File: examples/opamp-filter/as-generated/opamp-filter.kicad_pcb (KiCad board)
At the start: 2 copper layers, 58 x 42 mm, 22 parts, among them J1 IN, J2 5V, J3 OUT, U1 MCP6001R, U2 MCP6001R

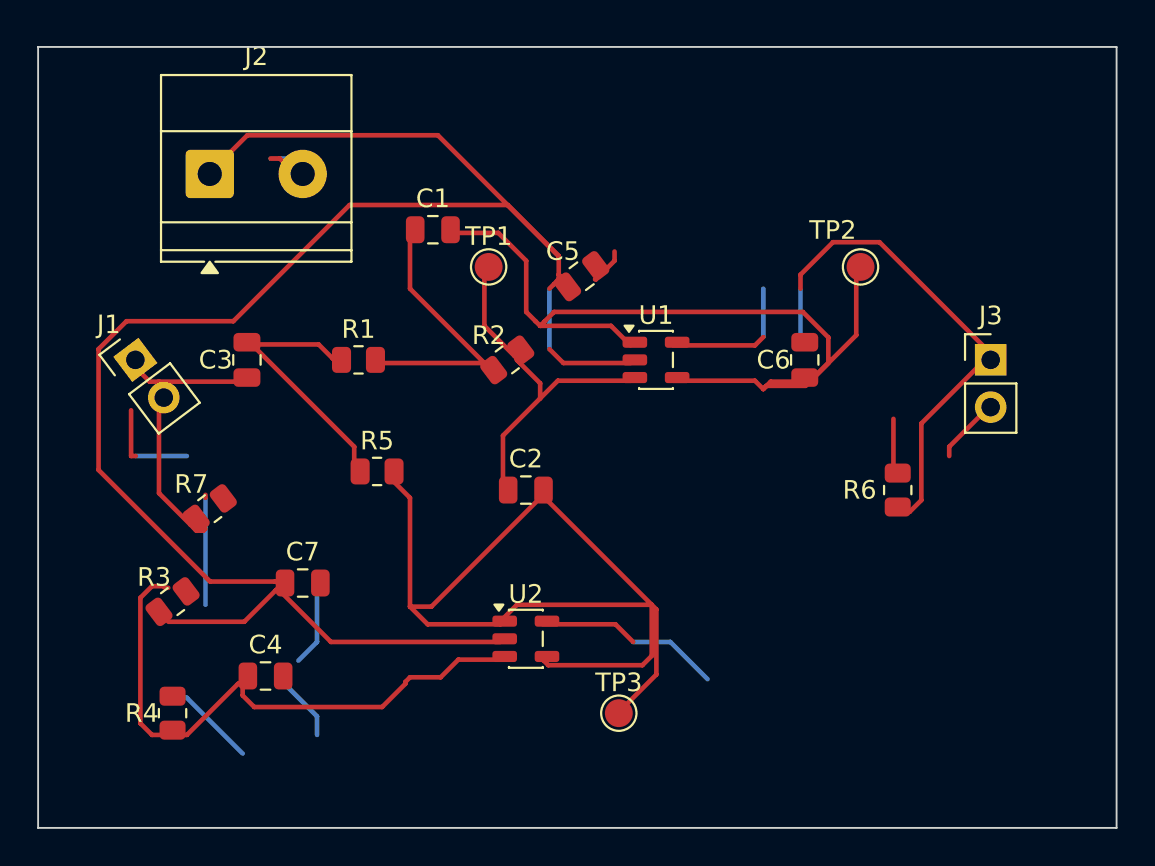
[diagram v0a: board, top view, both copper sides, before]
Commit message: Let a link finish on its own net's copper instead of the pad it names
Every junction on these boards sat on a pad, because a pad was the only
place the router was allowed to stop: a net with three branches funnelled
all three into one 0402, and the reviewer circled the result - converging
diagonals meeting on C15. People do not draw that; they tap the trunk at
the nearest point.

So the search may now end on any cell whose centre lies exactly on the
net's own copper (a tee), with two guards that took one broken board each
to learn: only copper already joined to the link's endpoint counts, or the
named pad is left unconnected; and only a pad-named endpoint may be teed
away from, because a link aimed at a bare coordinate is aimed at the
stated end of a trunk someone drew, and stopping short strands the
trunk's tail. A landing mid-segment is inserted into the trunk's points as
a stated corner, so the reshaping passes pin the join like any other.

The op-amp board shows the effect: 12% less copper, fewer corners, longer
strokes, same connectivity - DRC clean, gates clean, zero crossings on all
four regenerated boards.

Co-Authored-By: Claude Fable 5 <noreply@anthropic.com>
Claude-Session: https://claude.ai/code/session_01DUj7Ltu92tWg159mCSacwY
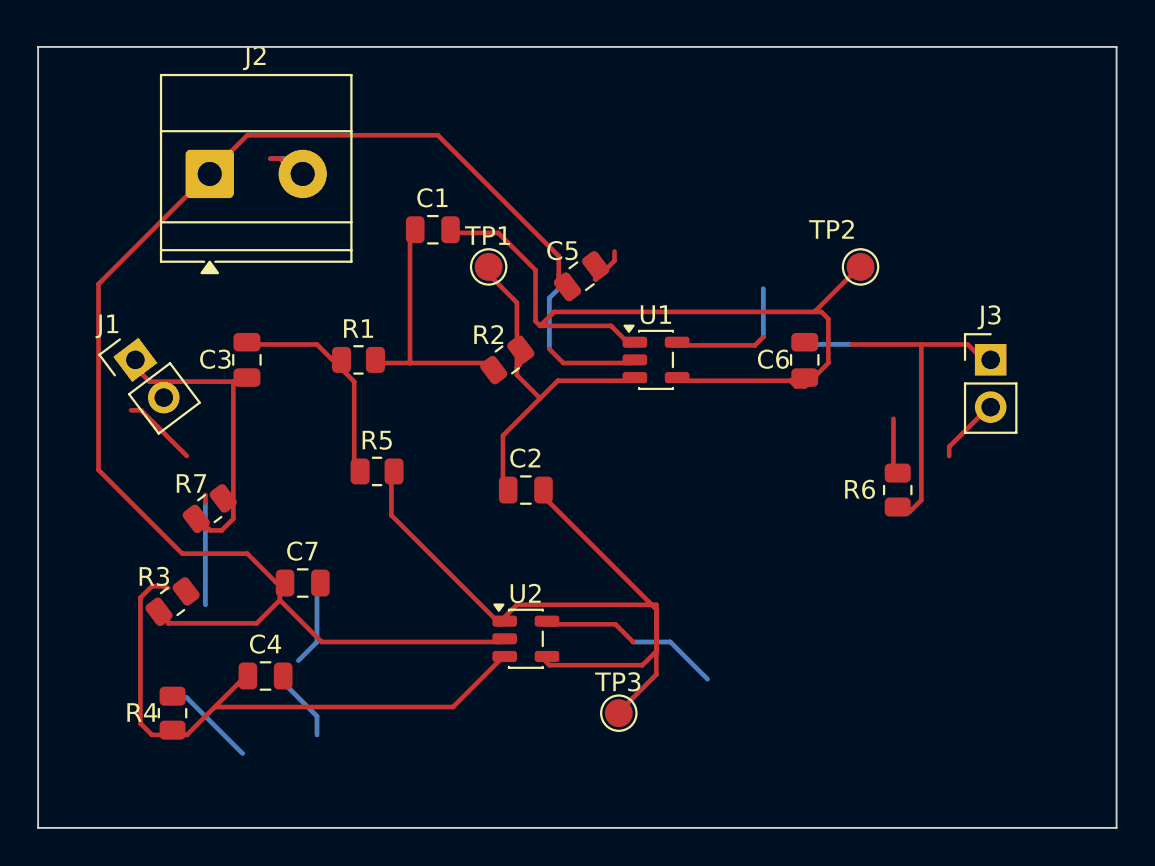
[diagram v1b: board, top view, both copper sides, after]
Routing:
- net +5V: track 100.9 -> 83.2 mm
- net /VREF: track 55.6 -> 44.1 mm
- net /OUT_AC: track 28.4 -> 20.6 mm
- net /OUT: track 50.7 -> 44.6 mm
- net /IN_DC: track 15.1 -> 12.4 mm
- net /X: track 14.9 -> 13.2 mm
- net GND: track 54.5 -> 53.0 mm

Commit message: Treat the ground plane as part of the drawing
Six reviewer circles, five of them the plane seen from different corners.
The pour now stops 1.2 mm inside the outline so an edge-hugging trace
keeps shell copper outside it; dead-end tongues narrower than 0.9 mm
retract instead of tapering to an acid-trap point in a bent corner; every
piece of the front pour over 8 mm2 holds a stitching via of its own,
placed before the orphan drop so a fenced-off strip gets a via instead of
staying a blank; and zone clearance comes down from 0.4 to 0.25, which is
what lets the plane flow between a 2.54 mm header's pins instead of
slotting the board top to bottom.

The round-twelve tee learns one manner: within two millimetres of the
goal it stands aside, so a rail flows through a bypass capacitor's pad
instead of feeding it by a stub - the carrier's bulk capacitor also moves
onto the VSYS run it was a millimetre south of. And
readability.margin_intrusion now measures symbol fields, power symbols
included: zero findings across KiCad's 18 demo sheets, one real catch on
our own motor sheet, whose power connector - like the FPGA board's -
moves in from the sheet edge so its printed name clears the frame.

Co-Authored-By: Claude Fable 5 <noreply@anthropic.com>
Claude-Session: https://claude.ai/code/session_01DUj7Ltu92tWg159mCSacwY
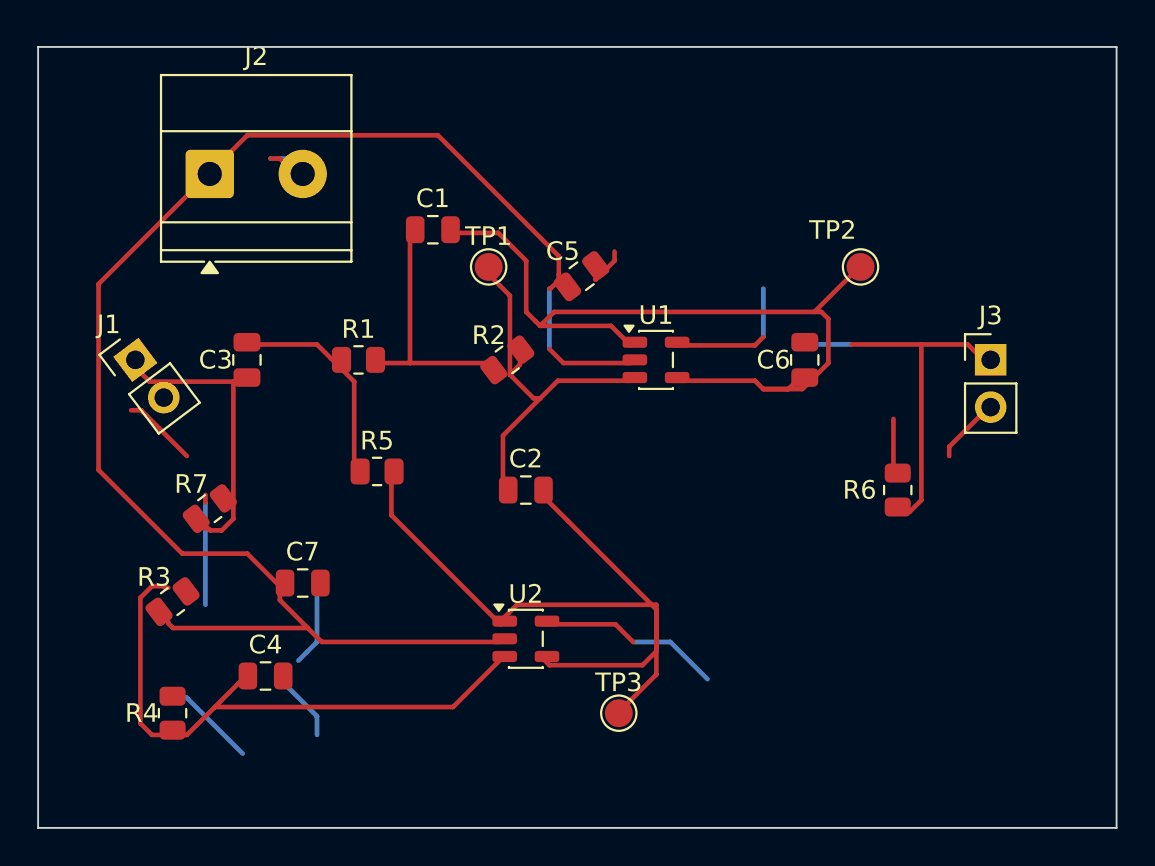
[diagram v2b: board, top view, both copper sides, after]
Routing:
- net /OUT: track 44.6 -> 46.9 mm
- net +5V: track 83.2 -> 84.3 mm
- net /FILT_IN: track 19.7 -> 20.4 mm
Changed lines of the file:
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@@
 	(segment (start 127.95 77.95) (end 127.0 78.9) (width 0.25) (layer "F.Cu") (net 3))
 	(segment (start 134.1375 77.95) (end 134.3675 77.95) (width 0.25) (layer "F.Cu") (net 7))
-	(segment (start 134.3675 77.95) (end 140.45 77.95) (width 0.25) (layer "F.Cu") (net 7))
-	(segment (start 140.45 77.95) (end 140.755 78.255) (width 0.25) (layer "F.Cu") (net 7))
-	(segment (start 140.755 78.255) (end 141.245 78.255) (width 0.25) (layer "F.Cu") (net 7))
-	(segment (start 141.245 78.255) (end 141.275 78.225) (width 0.25) (layer "F.Cu") (net 7))
-	(segment (start 141.275 78.225) (end 141.475 78.025) (width 0.25) (layer "F.Cu") (net 7))
-	(segment (start 141.475 78.025) (end 142.5 77.0) (width 0.25) (layer "F.Cu") (net 7))
-	(segment (start 142.5 77.0) (end 142.5 74.625) (width 0.25) (layer "F.Cu") (net 7))
-	(segment (start 142.5 74.625) (end 142.125 74.25) (width 0.25) (layer "F.Cu") (net 7))
-	(segment (start 142.125 74.25) (end 141.75 74.25) (width 0.25) (layer "F.Cu") (net 7))
+	(segment (start 134.3675 77.95) (end 138.55 77.95) (width 0.25) (layer "F.Cu") (net 7))
+	(segment (start 138.55 77.95) (end 139.0 78.4) (width 0.25) (layer "F.Cu") (net 7))
 	(segment (start 133.0 90.0) (end 125.75 90.0) (width 0.25) (layer "F.Cu") (net 9))
 	(segment (start 125.75 90.0) (end 125.0 90.75) (width 0.25) (layer "F.Cu") (net 9))
@@
 	(segment (start 118.9425 83.03) (end 118.9125 83.0) (width 0.25) (layer "F.Cu") (net 9))
 	(segment (start 124.8625 92.0) (end 115.25 92.0) (width 0.25) (layer "F.Cu") (net 2))
-	(segment (start 115.25 92.0) (end 113.0 89.75) (width 0.25) (layer "F.Cu") (net 2))
+	(segment (start 115.25 92.0) (end 114.5 91.25) (width 0.25) (layer "F.Cu") (net 2))
 	(segment (start 124.8625 92.95) (end 122.3125 95.5) (width 0.25) (layer "F.Cu") (net 6))
 	(segment (start 122.3125 95.5) (end 109.5 95.5) (width 0.25) (layer "F.Cu") (net 6))
@@
 	(segment (start 125.9125 77.0) (end 125.9125 77.0875) (width 0.25) (layer "F.Cu") (net 3))
 	(segment (start 125.9125 77.0875) (end 125.75 77.25) (width 0.25) (layer "F.Cu") (net 3))
-	(segment (start 125.75 77.25) (end 125.75 77.65) (width 0.25) (layer "F.Cu") (net 3))
-	(segment (start 125.75 77.65) (end 127.0 78.9) (width 0.25) (layer "F.Cu") (net 3))
+	(segment (start 125.75 77.25) (end 125.375 77.625) (width 0.25) (layer "F.Cu") (net 3))
+	(segment (start 127.0 78.9) (end 126.65 78.9) (width 0.25) (layer "F.Cu") (net 3))
+	(segment (start 126.65 78.9) (end 125.375 77.625) (width 0.25) (layer "F.Cu") (net 3))
 	(segment (start 124.0 72.0) (end 124.03 72.03) (width 0.25) (layer "F.Cu") (net 3))
-	(segment (start 124.03 72.03) (end 125.75 73.75) (width 0.25) (layer "F.Cu") (net 3))
-	(segment (start 125.75 73.75) (end 125.75 76.2808) (width 0.25) (layer "F.Cu") (net 3))
-	(segment (start 125.75 76.2808) (end 125.75 77.0) (width 0.25) (layer "F.Cu") (net 3))
-	(segment (start 125.75 77.0) (end 125.75 77.25) (width 0.25) (layer "F.Cu") (net 3))
+	(segment (start 124.03 72.03) (end 125.375 73.375) (width 0.25) (layer "F.Cu") (net 3))
+	(segment (start 125.375 73.375) (end 125.375 77.625) (width 0.25) (layer "F.Cu") (net 3))
 	(segment (start 144.0 72.0) (end 141.75 74.25) (width 0.25) (layer "F.Cu") (net 7))
 	(segment (start 131.0 96.0) (end 131.2 95.8) (width 0.25) (layer "F.Cu") (net 9))
@@
 	(segment (start 133.25 93.75) (end 133.25 90.25) (width 0.25) (layer "F.Cu") (net 9))
 	(segment (start 133.25 90.25) (end 133.0 90.0) (width 0.25) (layer "F.Cu") (net 9))
-	(segment (start 133.0 90.0) (end 127.5 84.5) (width 0.25) (layer "F.Cu") (net 9))
-	(segment (start 127.5 84.5) (end 127.25 84.25) (width 0.25) (layer "F.Cu") (net 9))
+	(segment (start 133.0 90.0) (end 128.5 85.5) (width 0.25) (layer "F.Cu") (net 9))
+	(segment (start 128.5 85.5) (end 127.25 84.25) (width 0.25) (layer "F.Cu") (net 9))
 	(segment (start 127.25 84.25) (end 127.2 84.25) (width 0.25) (layer "F.Cu") (net 9))
 	(segment (start 127.2 84.25) (end 126.98 84.03) (width 0.25) (layer "F.Cu") (net 9))
@@
 	(segment (start 127.0 75.0) (end 127.75 74.25) (width 0.25) (layer "F.Cu") (net 7))
 	(segment (start 127.75 74.25) (end 141.75 74.25) (width 0.25) (layer "F.Cu") (net 7))
+	(segment (start 141.75 74.25) (end 142.125 74.25) (width 0.25) (layer "F.Cu") (net 7))
+	(segment (start 142.125 74.25) (end 142.5 74.625) (width 0.25) (layer "F.Cu") (net 7))
+	(segment (start 142.5 74.625) (end 142.5 77.0) (width 0.25) (layer "F.Cu") (net 7))
+	(segment (start 142.5 77.0) (end 141.475 78.025) (width 0.25) (layer "F.Cu") (net 7))
+	(segment (start 141.475 78.025) (end 141.275 78.225) (width 0.25) (layer "F.Cu") (net 7))
+	(segment (start 141.275 78.225) (end 141.1 78.4) (width 0.25) (layer "F.Cu") (net 7))
+	(segment (start 141.1 78.4) (end 139.0 78.4) (width 0.25) (layer "F.Cu") (net 7))
 	(segment (start 127.0 75.0) (end 126.75 74.75) (width 0.25) (layer "F.Cu") (net 7))
-	(segment (start 126.75 74.75) (end 126.75 72.0) (width 0.25) (layer "F.Cu") (net 7))
-	(segment (start 126.75 72.0) (end 124.75 70.0) (width 0.25) (layer "F.Cu") (net 7))
+	(segment (start 126.75 74.75) (end 126.25 74.25) (width 0.25) (layer "F.Cu") (net 7))
+	(segment (start 126.25 74.25) (end 126.25 71.5) (width 0.25) (layer "F.Cu") (net 7))
+	(segment (start 126.25 71.5) (end 124.75 70.0) (width 0.25) (layer "F.Cu") (net 7))
 	(segment (start 124.75 70.0) (end 122.18 70.0) (width 0.25) (layer "F.Cu") (net 7))
 	(segment (start 122.18 70.0) (end 121.95 70.0) (width 0.25) (layer "F.Cu") (net 7))
+	(segment (start 139.0 78.4) (end 140.35 78.4) (width 0.25) (layer "F.Cu") (net 7))
+	(segment (start 140.35 78.4) (end 140.75 78.0) (width 0.25) (layer "F.Cu") (net 7))
+	(segment (start 140.75 78.0) (end 140.95 78.0) (width 0.25) (layer "F.Cu") (net 7))
+	(segment (start 140.95 78.0) (end 141.0 77.95) (width 0.25) (layer "F.Cu") (net 7))
 	(segment (start 141.0 76.05) (end 141.2 76.05) (width 0.25) (layer "F.Cu") (net 8))
 	(segment (start 141.2 76.05) (end 141.25 76.0) (width 0.25) (layer "F.Cu") (net 8))
@@
 	(segment (start 111.0 94.0) (end 110.75 94.25) (width 0.25) (layer "F.Cu") (net 6))
 	(segment (start 110.75 94.25) (end 109.5 95.5) (width 0.25) (layer "F.Cu") (net 6))
-	(segment (start 128.0 73.0) (end 128.0 72.9017) (width 0.25) (layer "F.Cu") (net 2))
-	(segment (start 128.0 72.9017) (end 128.0 72.75) (width 0.25) (layer "F.Cu") (net 2))
-	(segment (start 128.0 72.75) (end 128.0 72.55) (width 0.25) (layer "F.Cu") (net 2))
-	(segment (start 128.0 72.55) (end 128.05 72.5) (width 0.25) (layer "F.Cu") (net 2))
+	(segment (start 127.5 73.0) (end 127.55 73.0) (width 0.25) (layer "F.Cu") (net 2))
+	(segment (start 127.55 73.0) (end 128.05 72.5) (width 0.25) (layer "F.Cu") (net 2))
 	(segment (start 128.05 72.5) (end 128.0 72.45) (width 0.25) (layer "F.Cu") (net 2))
 	(segment (start 128.0 72.45) (end 128.0 72.25) (width 0.25) (layer "F.Cu") (net 2))
@@
 	(segment (start 113.0 89.05) (end 113.0 89.25) (width 0.25) (layer "F.Cu") (net 2))
 	(segment (start 113.0 89.25) (end 113.0 89.75) (width 0.25) (layer "F.Cu") (net 2))
-	(segment (start 127.5 76.25) (end 127.5 73.5) (width 0.25) (layer "B.Cu") (net 2))
-	(segment (start 127.5 73.5) (end 128.0 73.0) (width 0.25) (layer "B.Cu") (net 2))
+	(segment (start 113.0 89.75) (end 114.5 91.25) (width 0.25) (layer "F.Cu") (net 2))
+	(segment (start 127.5 76.25) (end 127.5 73.0) (width 0.25) (layer "B.Cu") (net 2))
 	(segment (start 107.0 90.9125) (end 107.0 91.0) (width 0.25) (layer "F.Cu") (net 2))
-	(segment (start 107.0 91.0) (end 111.75 91.0) (width 0.25) (layer "F.Cu") (net 2))
-	(segment (start 111.75 91.0) (end 113.0 89.75) (width 0.25) (layer "F.Cu") (net 2))
+	(segment (start 107.0 91.0) (end 107.25 91.25) (width 0.25) (layer "F.Cu") (net 2))
+	(segment (start 107.25 91.25) (end 114.5 91.25) (width 0.25) (layer "F.Cu") (net 2))
 )
